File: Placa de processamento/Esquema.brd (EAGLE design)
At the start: 145.1 x 89.8 mm, 12 parts

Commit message: Ajustes finalizados!
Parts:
- moved U$10 1.00 mm to (9.62, 16.5)
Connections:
- net V_BATTERY: now also U$10.PL1, U$10.PR1; no longer U$10.PL3, U$10.PR3
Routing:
- net N$7: track 225.4 -> 233.7 mm
- net V_BATTERY: track 19.9 -> 21.4 mm
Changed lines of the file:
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@@
 <elements>
 <element name="U$1" library="CRD" library_urn="urn:adsk.eagle:library:39051337" package="BMP390_FOOTPRINT" package3d_urn="urn:adsk.eagle:package:40965124/5" value="BMP390V1" x="43.561" y="19.812" smashed="yes"/>
-<element name="U$10" library="CRD" library_urn="urn:adsk.eagle:library:39051337" package="PRESSION_BUTTON_FOOTPRINT" package3d_urn="urn:adsk.eagle:package:43483815/3" value="PRESSION_BUTTON" x="8.62" y="16.51" smashed="yes" rot="R270"/>
+<element name="U$10" library="CRD" library_urn="urn:adsk.eagle:library:39051337" package="PRESSION_BUTTON_FOOTPRINT" package3d_urn="urn:adsk.eagle:package:43483815/3" value="PRESSION_BUTTON" x="9.62" y="16.51" smashed="yes" rot="R270"/>
 <element name="U$2" library="CRD" library_urn="urn:adsk.eagle:library:39051337" package="E22-400T30D_FOOTPRINT" package3d_urn="urn:adsk.eagle:package:40965099/4" value="E22-400T30D" x="121.92" y="73.66" smashed="yes" rot="R180"/>
 <element name="U$3" library="CRD" library_urn="urn:adsk.eagle:library:39051337" package="GPS_MODULE_FOOTPRINT" package3d_urn="urn:adsk.eagle:package:39608400/5" value="GPS_MODULE" x="71.12" y="26.67" smashed="yes"/>
@@
 <contactref element="IC1" pad="IN"/>
 <contactref element="U$11" pad="30"/>
-<wire x1="15.423" y1="44.633" x2="25.4" y2="54.61" width="1.5" layer="16"/>
+<wire x1="3.023" y1="33.733" x2="23.9" y2="54.61" width="1.5" layer="16"/>
 <wire x1="137.16" y1="54.61" x2="137.16" y2="48.26" width="1.5" layer="1"/>
 <via x="137.16" y="48.26" extent="1-16" drill="0.7" diameter="1.3"/>
@@
 <wire x1="132.28" y1="10.36" x2="128.28" y2="10.36" width="1.5" layer="16"/>
 <wire x1="137.16" y1="15.24" x2="132.28" y2="10.36" width="1.5" layer="16"/>
-<wire x1="25.4" y1="54.61" x2="52.88" y2="54.61" width="1.5" layer="16"/>
+<wire x1="23.9" y1="54.61" x2="52.88" y2="54.61" width="1.5" layer="16"/>
 <wire x1="52.88" y1="54.61" x2="59.69" y2="54.61" width="1.5" layer="16"/>
 <via x="99.06" y="57.15" extent="1-16" drill="0.7" diameter="1.3"/>
@@
 <wire x1="94.25" y1="61.96" x2="99.06" y2="57.15" width="1.5" layer="16"/>
 <wire x1="94.25" y1="61.96" x2="60.23" y2="61.96" width="1.5" layer="16"/>
-<wire x1="15.423" y1="24.313" x2="15.423" y2="44.633" width="1.5" layer="16"/>
+<wire x1="10.818" y1="21.313" x2="5.818" y2="21.313" width="1.5" layer="16"/>
+<wire x1="5.818" y1="21.313" x2="3.023" y2="24.108" width="1.5" layer="16"/>
+<wire x1="3.023" y1="33.733" x2="3.023" y2="24.108" width="1.5" layer="16"/>
 <wire x1="52.88" y1="54.61" x2="60.23" y2="61.96" width="1.5" layer="16"/>
 <wire x1="59.69" y1="54.61" x2="63.5" y2="58.42" width="1.5" layer="16"/>
@@
 <contactref element="U$10" pad="PR2"/>
 <contactref element="U$10" pad="PL2"/>
-<wire x1="7.318" y1="21.313" x2="9.818" y2="21.313" width="1.5" layer="16"/>
-<wire x1="9.818" y1="21.313" x2="9.841" y2="21.29" width="1.5" layer="16"/>
-<wire x1="12.4" y1="21.29" x2="9.841" y2="21.29" width="1.5" layer="16"/>
-<wire x1="12.4" y1="21.29" x2="15.423" y2="24.313" width="1.5" layer="16"/>
+<wire x1="8.318" y1="21.313" x2="10.818" y2="21.313" width="1.5" layer="16"/>
 </signal>
 <signal name="N$12">
@@
 <signal name="V_BATTERY">
 <contactref element="U$7" pad="1"/>
-<wire x1="23.59" y1="13.97" x2="25.4" y2="13.97" width="1.5" layer="16"/>
-<contactref element="U$10" pad="PL3"/>
-<contactref element="U$10" pad="PR3"/>
-<wire x1="19.247" y1="18.313" x2="23.59" y2="13.97" width="1.5" layer="16"/>
-<wire x1="7.318" y1="18.313" x2="9.818" y2="18.313" width="1.5" layer="16"/>
-<wire x1="9.818" y1="18.313" x2="19.247" y2="18.313" width="1.5" layer="16"/>
+<contactref element="U$10" pad="PR1"/>
+<contactref element="U$10" pad="PL1"/>
+<wire x1="8.318" y1="24.313" x2="10.818" y2="24.313" width="1.5" layer="16"/>
+<wire x1="10.818" y1="24.313" x2="12.687" y2="24.313" width="1.5" layer="16"/>
+<wire x1="23.03" y1="13.97" x2="25.4" y2="13.97" width="1.5" layer="16"/>
+<wire x1="12.687" y1="24.313" x2="23.03" y2="13.97" width="1.5" layer="16"/>
 </signal>
 <signal name="N$19">

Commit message: Atualização
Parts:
- removed IC1: (no value), v-reg:78LXX
- added IC2: (no value), v-reg:78XXL
- moved U$3 0.10 mm to (71.2, 26.7), flipped to the bottom
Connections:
- net GND: now also IC2.GND; no longer IC1.GND
- net N$12: now also IC2.OUT; no longer IC1.OUT
- net N$7: now also IC2.IN; no longer IC1.IN
- net N$8: now also U$2.RXD; no longer U$2.TXD
- net N$9: now also U$2.TXD; no longer U$2.RXD
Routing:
- net GND: track 350.3 -> 254.1 mm, vias 8 -> 7
- net N$3: track 201.5 -> 214.8 mm, vias 4 -> 6
- net N$6: track 68.0 -> 64.8 mm, vias 2 -> 0
- net N$12: track 81.8 -> 84.8 mm
- net N$7: track 233.7 -> 231.2 mm
- net N$9: track 49.6 -> 51.5 mm
- net N$20: track 120.8 -> 119.1 mm
- net N$5: track 61.7 -> 63.1 mm
- net N$8: track 54.4 -> 54.1 mm, vias 0 -> 2

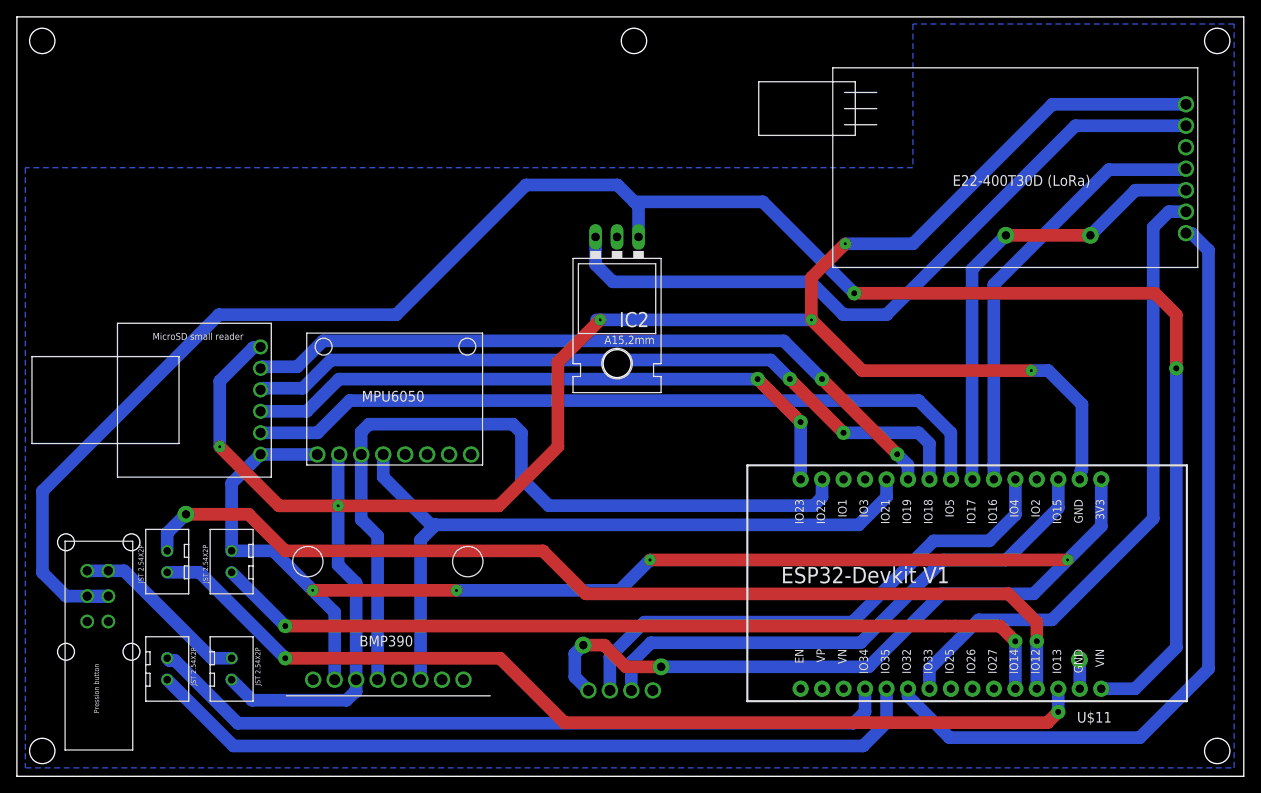
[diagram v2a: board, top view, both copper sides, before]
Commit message: Adicionado plano de terra no top - Joliot processamento.
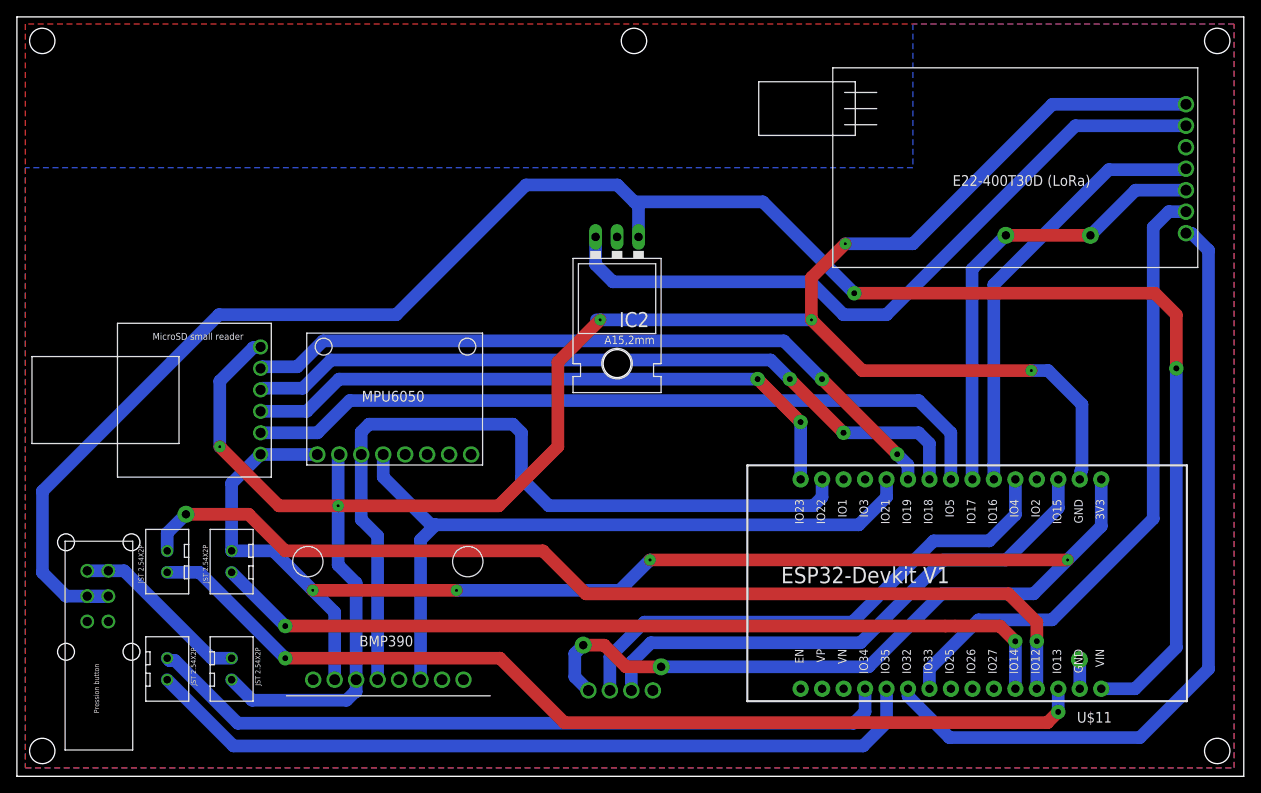
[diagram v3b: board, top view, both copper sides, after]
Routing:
- added copper zone on layer 1, net GND
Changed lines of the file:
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@@
 <wire x1="125.74" y1="13.76" x2="125.7" y2="13.8" width="1.5" layer="16"/>
 <via x="125.7" y="13.8" extent="1-16" drill="1" diameter="1.3"/>
-<wire x1="125.74" y1="35.13" x2="125.7" y2="13.8" width="0" layer="19" extent="1-1"/>
-<wire x1="75.23" y1="10.16" x2="40.132" y2="11.43" width="0" layer="19" extent="1-1"/>
+<polygon width="0.1524" layer="1">
+<vertex x="1" y="89"/>
+<vertex x="1" y="1"/>
+<vertex x="144" y="1"/>
+<vertex x="144" y="89"/>
+</polygon>
 </signal>
 </signals>

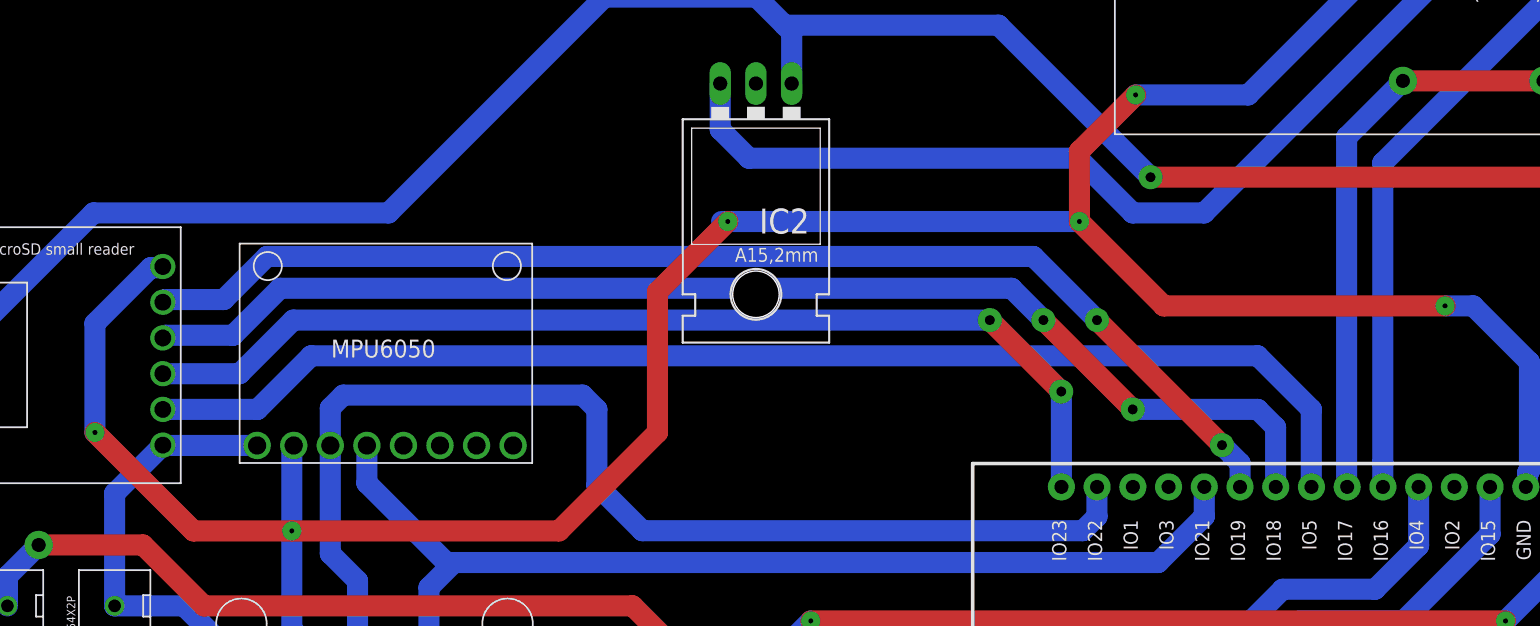
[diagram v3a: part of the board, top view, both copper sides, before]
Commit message: Adicionado plano de terra no top - Joliot processamento.
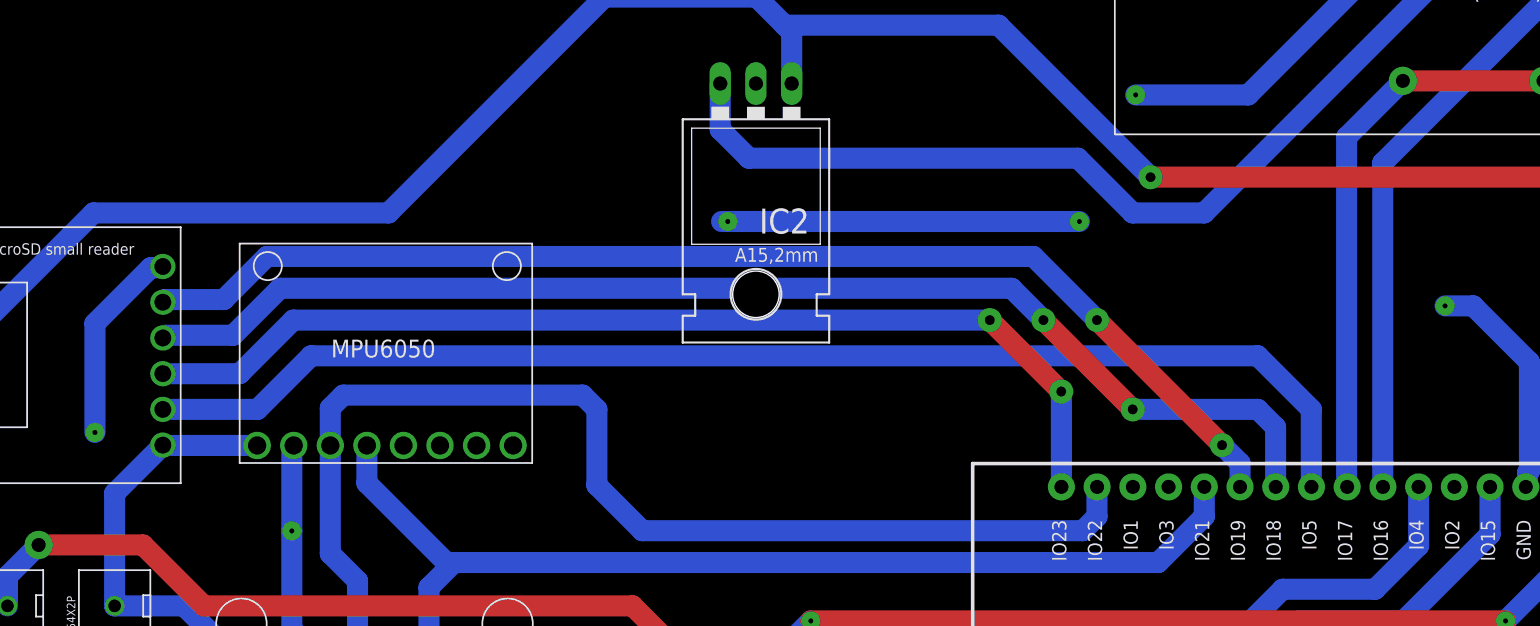
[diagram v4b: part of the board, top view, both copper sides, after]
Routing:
- net GND: track 254.1 -> 152.1 mm
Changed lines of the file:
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@@
 <contactref element="U$2" pad="GND"/>
 <wire x1="40.132" y1="11.43" x2="40.132" y2="22.868" width="1.5" layer="16"/>
-<wire x1="94" y1="54" x2="100" y2="48" width="1.5" layer="1"/>
 <wire x1="68.555" y1="54" x2="69" y2="54" width="1.5" layer="16"/>
 <wire x1="69" y1="54" x2="94" y2="54" width="1.5" layer="16"/>
-<wire x1="100" y1="48" x2="120" y2="48" width="1.5" layer="1"/>
 <via x="120" y="48" extent="1-16" drill="0.35"/>
 <wire x1="120" y1="48" x2="122" y2="48" width="1.5" layer="16"/>
@@
 <wire x1="125.8648" y1="35.2548" x2="125.74" y2="35.13" width="1.5" layer="16"/>
 <via x="69" y="54" extent="1-16" drill="0.35"/>
-<wire x1="69" y1="54" x2="64" y2="49" width="1.5" layer="1"/>
 <via x="94" y="54" extent="1-16" drill="0.35"/>
-<wire x1="94" y1="54" x2="94" y2="59" width="1.5" layer="1"/>
-<wire x1="94" y1="59" x2="98" y2="63" width="1.5" layer="1"/>
 <via x="98" y="63" extent="1-16" drill="0.35"/>
 <wire x1="138.303" y1="79.502" x2="122.502" y2="79.502" width="1.5" layer="16"/>
 <wire x1="122.502" y1="79.502" x2="106" y2="63" width="1.5" layer="16"/>
 <wire x1="106" y1="63" x2="98" y2="63" width="1.5" layer="16"/>
-<wire x1="64" y1="39" x2="64" y2="49" width="1.5" layer="1"/>
 <wire x1="38" y1="25" x2="38" y2="32" width="1.5" layer="16"/>
 <wire x1="40.132" y1="22.868" x2="38" y2="25" width="1.5" layer="16"/>
 <via x="38" y="32" extent="1-16" drill="0.35"/>
-<wire x1="38" y1="32" x2="57" y2="32" width="1.5" layer="1"/>
-<wire x1="57" y1="32" x2="64" y2="39" width="1.5" layer="1"/>
 <wire x1="38" y1="32" x2="38" y2="37.94" width="1.5" layer="16"/>
 <wire x1="38" y1="37.94" x2="38.1355" y2="38.0755" width="1.5" layer="16"/>
@@
 <wire x1="24" y1="46.75440625" x2="24" y2="39" width="1.5" layer="16"/>
 <via x="24" y="39" extent="1-16" drill="0.35"/>
-<wire x1="24" y1="39" x2="31" y2="32" width="1.5" layer="1"/>
-<wire x1="31" y1="32" x2="38" y2="32" width="1.5" layer="1"/>
 <contactref element="U$3" pad="GND"/>
 <wire x1="40.132" y1="10" x2="40.132" y2="11.43" width="1.5" layer="16"/>
